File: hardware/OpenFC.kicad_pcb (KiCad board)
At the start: 6 copper layers, 27.6 x 27.6 mm, 135 parts, among them J10 5V, J12 5V, J14 5V, J15 5V, J17 5V, J18 5V, J20 5V, J21 5V, J22 5V, J24 5V, J25 5V, J26 5V, J27 5V, J28 5V, J29 5V, J30 5V, J31 5V, J32 5V, J33 5V, J34 5V, J35 5V, J37 5V, J39 5V, J40 5V, J41 5V, J42 5V, J43 5V, J44 5V, J45 5V, J46 5V, J48 5V, J49 5V, J5 5V, J8 5V, P1 SM08B-SRSS-TB(LF)(SN), Q5 AP1606, Q6 AP1606, U1 COS8051SOT, U10 RP2354A, U11 TS2306A 240GF MSM 9_C2976675, U18 SN74LVC1G3157DTBR, U2 TLV7031DPWR, U3 TI LMR51430YFDDCR, U4 TI LMR51430YFDDCR, U5 TPS2116DRLR, U6 NCV8187AMT180TAG, U7 LP5912-3.3DRVR, U8 SM06B-SRSS-TB(LF)(SN), U9 LSM6DSV16XTR, X1 XTM25012000JT00351001

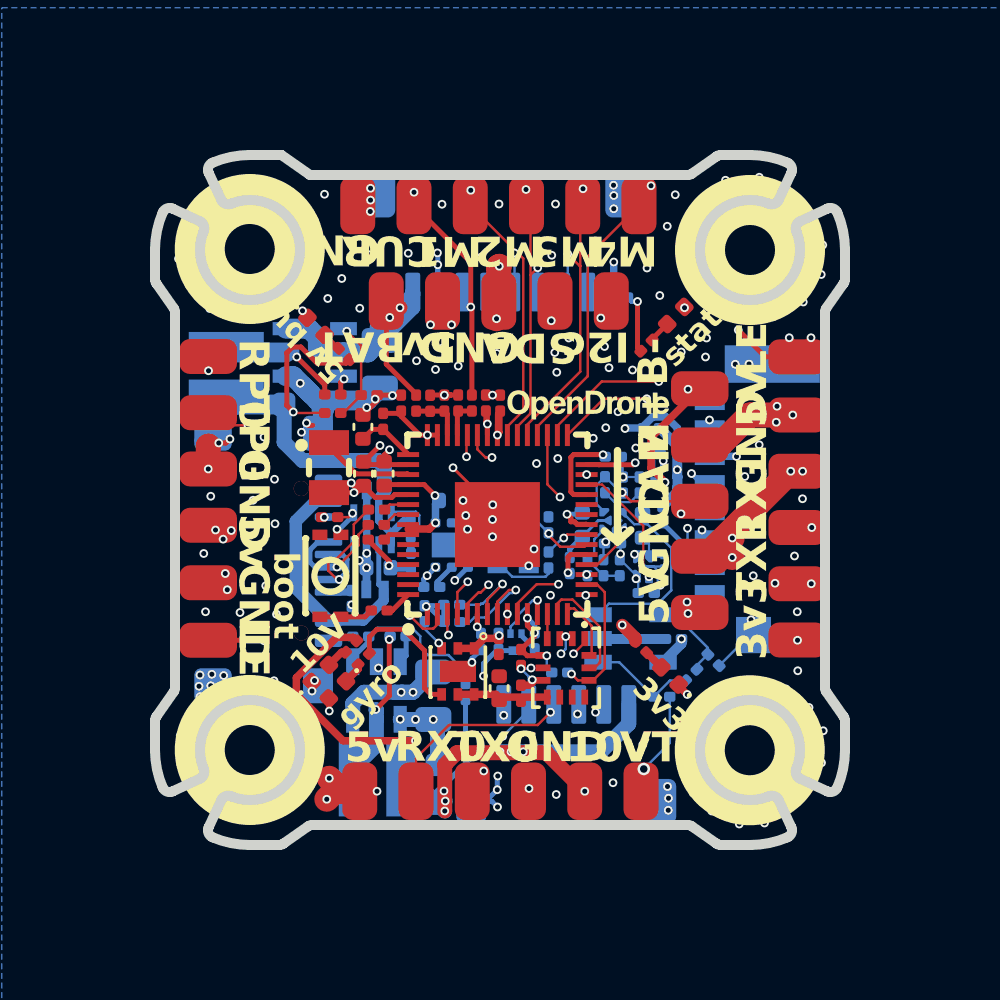
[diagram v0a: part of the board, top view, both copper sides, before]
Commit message: Swap 1.8V LDO and IMU, fix BOM/CPL export hygiene
Part changes, both schematic and PCB:
- U6 NCV8187AMT180TAG (stock 0 at JLC) replaced by U12 LP5912-1.8DRVR
  (C2876234). Same WSON-6 2x2 land pattern as the LP5912-3.3 at U7, so no
  layout change. PG is retained. PSRR at the 1 mA gyro load is ~85 dB to
  1 kHz and ~70 dB at 10 kHz per datasheet Figure 23.
- PG indicator rewired: pull-up from +5V to PG, LED from PG to GND, so the
  LED lights when the rail is good instead of when it has failed.
- U9 LSM6DSV16XTR replaced by BMI270 (C2836813). Bosch Table 22 matches the
  existing LGA-14 symbol pin for pin, so no rewire and no CPL rotation change.
- C33, C34 22uF 0402 moved from C105226 to C415703.

Export fixes:
- U12 carried its part number in a field named "LCSC Part" rather than
  "LCSC", so it exported with no part number and would have been quoted
  unsourced. Renamed.
- The 34 solder pad and testpoint footprints now carry exclude_from_bom
  plus exclude_from_pos_files instead of relying on the dnp flag. They stay
  on the board as copper but no longer need --exclude-dnp at export time.

BOM and CPL now agree at 101 placements with no blank part numbers, exported
without any dnp flag. ERC is unchanged against HEAD (170 vs 171 violations,
all pre-existing).

Co-Authored-By: Claude Fable 5 <noreply@anthropic.com>
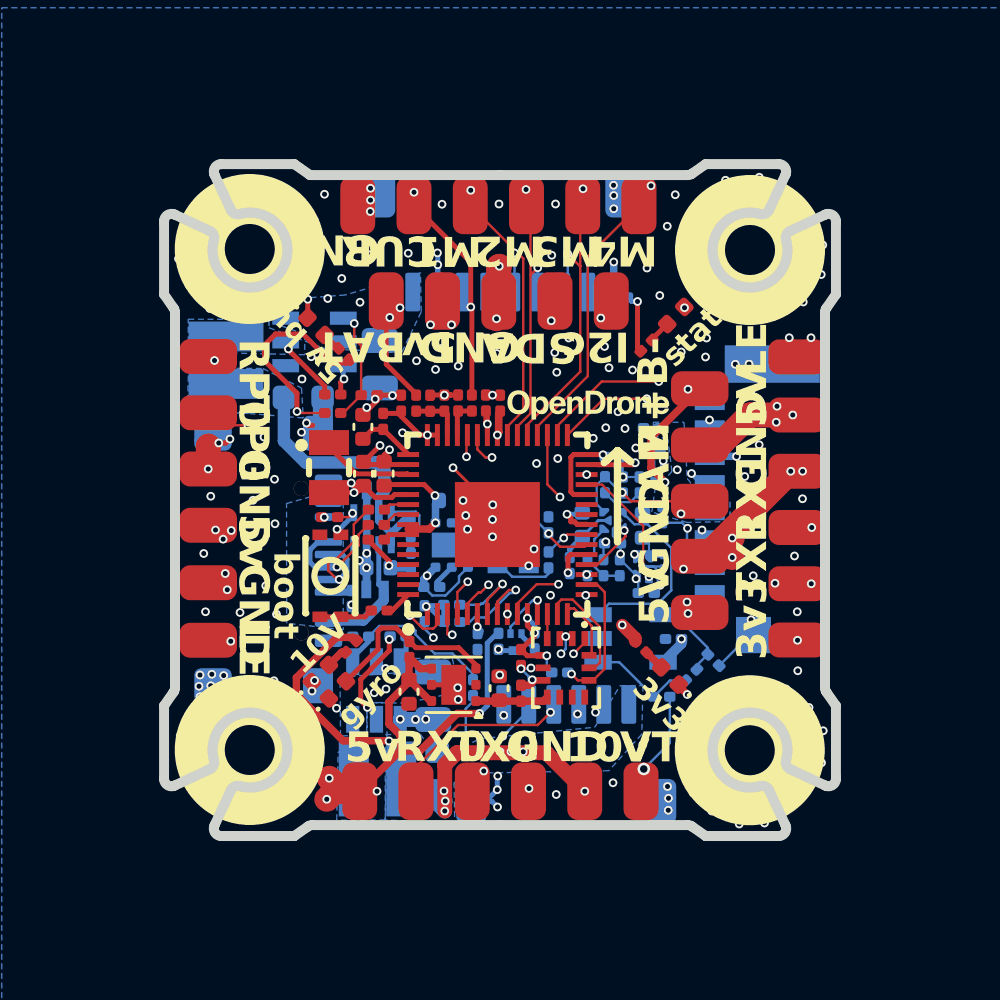
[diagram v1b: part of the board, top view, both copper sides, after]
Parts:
- removed R40: 2.4k, Resistor_SMD:R_0201_0603Metric
- removed U6: NCV8187AMT180TAG, lib:WDFN-6_L2.0-W2.0-P0.65-BL-EP
- added R34: 6.49k, Resistor_SMD:R_0201_0603Metric, F.Cu at (149.0, 92.5)
- added U12: LP5912-1.8DRVR, lib:WSON-6-1EP_2x2mm_P0.65mm_EP1x1.6mm_ThermalVias, F.Cu at (150.8, 93.9)
- C31: value 100n -> 4.7uF; footprint Capacitor_SMD:C_0201_0603Metric -> Capacitor_SMD:C_0402_1005Metric
- U9: value LSM6DSV16XTR -> BMI270
- moved C31 4.02 mm to (149.0, 94.2)
- moved C28 0.53 mm to (150.1, 97.3)
- moved L3 0.42 mm to (141.7, 80.9)
- moved U4 0.42 mm to (145.2, 80.2)
- moved R29 0.34 mm to (151.5, 94.0)
- moved C29 0.28 mm to (144.7, 82.4)
- moved C3 0.14 mm to (151.7, 92.2)
- turned D8 to 45 degrees
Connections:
- D8 pad 1: Net-(D8-K) -> GND
- D8 pad 2: +5V -> /POWER/1.8V_PG
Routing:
- net +BATT: track 39.5 -> 23.9 mm
- net GND: track 94.7 -> 80.3 mm, vias 182 -> 188
- net +10V: track 34.1 -> 19.7 mm
- net +5V: track 38.2 -> 49.5 mm, vias 21 -> 18
- net +5V_USB: track 11.0 -> 4.85 mm
- net +3.3V: track 43.2 -> 37.9 mm
- net /PADS/LED_STRIP: track 57.8 -> 54.0 mm, vias 5 -> 4
- net Net-(U3-SW): track 6.33 -> 3.44 mm
- net Net-(U4-SW): track 4.45 -> 2.42 mm
- net /POWER/1.8V_PG: track 5.64 -> 7.26 mm
- net /BLACKBOX/FLASH_CS: track 13.7 -> 12.2 mm
- net Net-(D8-K): track 0.86 -> 0.00 mm
- net +1.8V_GYRO: track 3.62 -> 2.92 mm
- net Net-(U4-CB): track 0.67 -> 1.22 mm
- net +5V_BUCK: track 19.5 -> 19.0 mm
- added copper zone on B.Cu, net +10V
- added copper zone on B.Cu, net +3.3V
- added copper zone on B.Cu, net +5V_BUCK
- added copper zone on B.Cu, net +5V_USB
- added copper zone on B.Cu, net +BATT
- added copper zone on B.Cu, net Net-(U3-SW)
- added copper zone on B.Cu, net Net-(U4-SW)
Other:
- board size 27.6 x 27.6 mm -> 26.9 x 26.9 mm

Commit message: Rev 3: LP5912 gyro LDO, BMI270
Gyro supply moves to LP5912-1.8DRVR (U12, C2876234); the NCV8187AMT180TAG is
gone from schematic and board. IMU is BMI270 (U9). Bucks stay LMR51430YFDDCR,
which has adequate margin for the 6S ceiling this board shares with the 20x20
ESC.

ERC and DRC reviewed by the maintainer.

Co-Authored-By: Claude Opus 5 (1M context) <noreply@anthropic.com>
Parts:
- U3, U4: value TI LMR51430YFDDCR -> LMR51430YFDDCR
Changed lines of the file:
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@@
 			)
 		)
-		(attr smd exclude_from_pos_files exclude_from_bom)
+		(attr smd exclude_from_bom dnp)
 		(duplicate_pad_numbers_are_jumpers no)
 		(fp_text user "${REFERENCE}"
@@
 			)
 		)
-		(attr smd exclude_from_pos_files exclude_from_bom)
+		(attr smd exclude_from_bom dnp)
 		(duplicate_pad_numbers_are_jumpers no)
 		(fp_text user "${REFERENCE}"
@@
 			)
 		)
-		(attr smd exclude_from_pos_files exclude_from_bom)
+		(attr smd exclude_from_bom dnp)
 		(duplicate_pad_numbers_are_jumpers no)
 		(fp_text user "${REFERENCE}"
@@
 			)
 		)
-		(attr smd exclude_from_pos_files exclude_from_bom)
+		(attr smd exclude_from_bom dnp)
 		(duplicate_pad_numbers_are_jumpers no)
 		(fp_text user "${REFERENCE}"
@@
 			)
 		)
-		(attr smd exclude_from_pos_files exclude_from_bom)
+		(attr smd exclude_from_bom dnp)
 		(duplicate_pad_numbers_are_jumpers no)
 		(fp_text user "${REFERENCE}"
@@
 			)
 		)
-		(attr smd exclude_from_pos_files exclude_from_bom)
+		(attr smd exclude_from_bom dnp)
 		(duplicate_pad_numbers_are_jumpers no)
 		(fp_text user "${REFERENCE}"
@@
 			)
 		)
-		(attr smd exclude_from_pos_files exclude_from_bom)
+		(attr smd exclude_from_bom dnp)
 		(duplicate_pad_numbers_are_jumpers no)
 		(fp_text user "${REFERENCE}"
@@
 			)
 		)
-		(attr smd exclude_from_pos_files exclude_from_bom)
+		(attr smd exclude_from_bom dnp)
 		(duplicate_pad_numbers_are_jumpers no)
 		(fp_text user "${REFERENCE}"
@@
 			)
 		)
-		(attr smd exclude_from_pos_files exclude_from_bom)
+		(attr smd exclude_from_bom dnp)
 		(duplicate_pad_numbers_are_jumpers no)
 		(fp_text user "${REFERENCE}"
@@
 			)
 		)
-		(attr smd exclude_from_pos_files exclude_from_bom)
+		(attr smd exclude_from_bom dnp)
 		(duplicate_pad_numbers_are_jumpers no)
 		(fp_text user "${REFERENCE}"
@@
 			)
 		)
-		(attr smd exclude_from_pos_files exclude_from_bom)
+		(attr smd exclude_from_bom dnp)
 		(duplicate_pad_numbers_are_jumpers no)
 		(fp_text user "${REFERENCE}"
@@
 			)
 		)
-		(attr smd exclude_from_pos_files exclude_from_bom)
+		(attr smd exclude_from_bom dnp)
 		(duplicate_pad_numbers_are_jumpers no)
 		(fp_text user "${REFERENCE}"
@@
 			)
 		)
+		(property "LCSC" "C2876234"
+			(at 0 0 180)
+			(unlocked yes)
+			(layer "F.Fab")
+			(hide yes)
+			(effects
+				(font
+					(size 1 1)
+					(thickness 0.15)
+				)
+			)
+		)
 		(sheetname "/POWER/")
 		(sheetfile "power.kicad_sch")
@@
 			)
 		)
-		(attr smd exclude_from_pos_files exclude_from_bom)
+		(attr smd exclude_from_bom dnp)
 		(duplicate_pad_numbers_are_jumpers no)
 		(fp_text user "${REFERENCE}"
@@
 			)
 		)
-		(attr smd exclude_from_pos_files exclude_from_bom)
+		(attr smd exclude_from_bom dnp)
 		(duplicate_pad_numbers_are_jumpers no)
 		(fp_text user "${REFERENCE}"
@@
 			)
 		)
-		(attr smd exclude_from_pos_files exclude_from_bom)
+		(attr smd exclude_from_bom dnp)
 		(duplicate_pad_numbers_are_jumpers no)
 		(fp_text user "${REFERENCE}"
@@
 			)
 		)
-		(attr smd exclude_from_pos_files exclude_from_bom)
+		(attr smd exclude_from_bom dnp)
 		(duplicate_pad_numbers_are_jumpers no)
 		(fp_text user "${REFERENCE}"
@@
 			)
 		)
-		(attr smd exclude_from_pos_files exclude_from_bom)
+		(attr smd exclude_from_bom dnp)
 		(duplicate_pad_numbers_are_jumpers no)
 		(fp_text user "${REFERENCE}"
@@
 			)
 		)
-		(attr smd exclude_from_pos_files exclude_from_bom)
+		(attr smd exclude_from_bom dnp)
 		(duplicate_pad_numbers_are_jumpers no)
 		(fp_text user "${REFERENCE}"
@@
 			)
 		)
-		(attr smd exclude_from_pos_files exclude_from_bom)
+		(attr smd exclude_from_bom dnp)
 		(duplicate_pad_numbers_are_jumpers no)
 		(fp_text user "${REFERENCE}"
@@
 			)
 		)
-		(attr smd exclude_from_pos_files exclude_from_bom)
+		(attr smd exclude_from_bom dnp)
 		(duplicate_pad_numbers_are_jumpers no)
 		(fp_text user "${REFERENCE}"
@@
 			)
 		)
-		(attr smd exclude_from_pos_files exclude_from_bom)
+		(attr smd exclude_from_bom dnp)
 		(duplicate_pad_numbers_are_jumpers no)
 		(fp_text user "${REFERENCE}"
@@
 			)
 		)
-		(attr smd exclude_from_pos_files exclude_from_bom)
+		(attr smd exclude_from_bom dnp)
 		(duplicate_pad_numbers_are_jumpers no)
 		(fp_text user "${REFERENCE}"
@@
 			)
 		)
-		(attr smd exclude_from_pos_files exclude_from_bom)
+		(attr smd exclude_from_bom dnp)
 		(duplicate_pad_numbers_are_jumpers no)
 		(fp_text user "${REFERENCE}"
@@
 			)
 		)
-		(attr smd exclude_from_pos_files exclude_from_bom)
+		(attr smd exclude_from_bom dnp)
 		(duplicate_pad_numbers_are_jumpers no)
 		(fp_text user "${REFERENCE}"
@@
 			)
 		)
-		(attr smd exclude_from_pos_files exclude_from_bom)
+		(attr smd exclude_from_bom dnp)
 		(duplicate_pad_numbers_are_jumpers no)
 		(fp_text user "${REFERENCE}"
@@
 			)
 		)
-		(attr smd exclude_from_pos_files exclude_from_bom)
+		(attr smd exclude_from_bom dnp)
 		(duplicate_pad_numbers_are_jumpers no)
 		(fp_text user "${REFERENCE}"
@@
 			)
 		)
-		(attr smd exclude_from_pos_files exclude_from_bom)
+		(attr smd exclude_from_bom dnp)
 		(duplicate_pad_numbers_are_jumpers no)
 		(fp_text user "${REFERENCE}"
@@
 			)
 		)
-		(attr smd exclude_from_pos_files exclude_from_bom)
+		(attr smd exclude_from_bom dnp)
 		(duplicate_pad_numbers_are_jumpers no)
 		(fp_text user "${REFERENCE}"
@@
 			)
 		)
-		(attr smd exclude_from_pos_files exclude_from_bom)
+		(attr smd exclude_from_bom dnp)
 		(duplicate_pad_numbers_are_jumpers no)
 		(fp_text user "${REFERENCE}"
@@
 			)
 		)
-		(attr smd exclude_from_pos_files exclude_from_bom)
+		(attr smd exclude_from_bom dnp)
 		(duplicate_pad_numbers_are_jumpers no)
 		(fp_text user "${REFERENCE}"
@@
 			)
 		)
-		(attr smd exclude_from_pos_files exclude_from_bom)
+		(attr smd exclude_from_bom dnp)
 		(duplicate_pad_numbers_are_jumpers no)
 		(fp_text user "${REFERENCE}"
@@
 			)
 		)
-		(attr smd exclude_from_pos_files exclude_from_bom)
+		(attr smd exclude_from_bom dnp)
 		(duplicate_pad_numbers_are_jumpers no)
 		(fp_text user "${REFERENCE}"
@@
 			)
 		)
-		(attr smd exclude_from_pos_files exclude_from_bom)
+		(attr smd exclude_from_bom dnp)
 		(duplicate_pad_numbers_are_jumpers no)
 		(fp_text user "${REFERENCE}"
@@
 			)
 		)
-		(attr smd exclude_from_pos_files exclude_from_bom)
+		(attr smd exclude_from_bom dnp)
 		(duplicate_pad_numbers_are_jumpers no)
 		(fp_text user "${REFERENCE}"
@@
 			)
 		)
-		(property "Value" "TI LMR51430YFDDCR"
+		(property "Value" "LMR51430YFDDCR"
 			(at 0 -5.15 90)
 			(layer "B.Fab")
@@
 			)
 		)
-		(property "LCSC" "C5219261"
+		(property "LCSC" "C45262770"
 			(at 0 0 270)
 			(unlocked yes)
@@
 			)
 		)
-		(property "MPN" "TI LMR51430YFDDCR"
+		(property "MPN" "LMR51430YFDDCR"
 			(at 0 0 270)
 			(unlocked yes)
@@
 		(model "${KIPRJMOD}/lib.3dshapes/DFN-3L_L1.0-W0.6-H0.5-P0.65-BR.wrl"
 			(offset
-				(xyz 0.01 -0 0.5)
+				(xyz 0.01 0 0)
 			)
 			(scale
@@
 			)
 		)
-		(property "Value" "TI LMR51430YFDDCR"
+		(property "Value" "LMR51430YFDDCR"
 			(at 0 -5.15 0)
 			(layer "B.Fab")
@@
 			)
 		)
-		(property "LCSC" "C5219261"
+		(property "LCSC" "C45262770"
 			(at 0 0 0)
 			(unlocked yes)
@@
 			)
 		)
-		(property "MPN" "TI LMR51430YFDDCR"
+		(property "MPN" "LMR51430YFDDCR"
 			(at 0 0 0)
 			(unlocked yes)
@@
 		(model "${KIPRJMOD}/lib.3dshapes/SOD-882_L1.0-W0.6-H0.5-LS0.65.wrl"
 			(offset
-				(xyz -911.61 887.73 0)
+				(xyz 0 0 0)
 			)
 			(scale
@@
 		(model "${KIPRJMOD}/lib.3dshapes/SOD-882_L1.0-W0.6-H0.5-LS0.65.wrl"
 			(offset
-				(xyz -911.61 887.73 0)
+				(xyz 0 0 0)
 			)
 			(scale

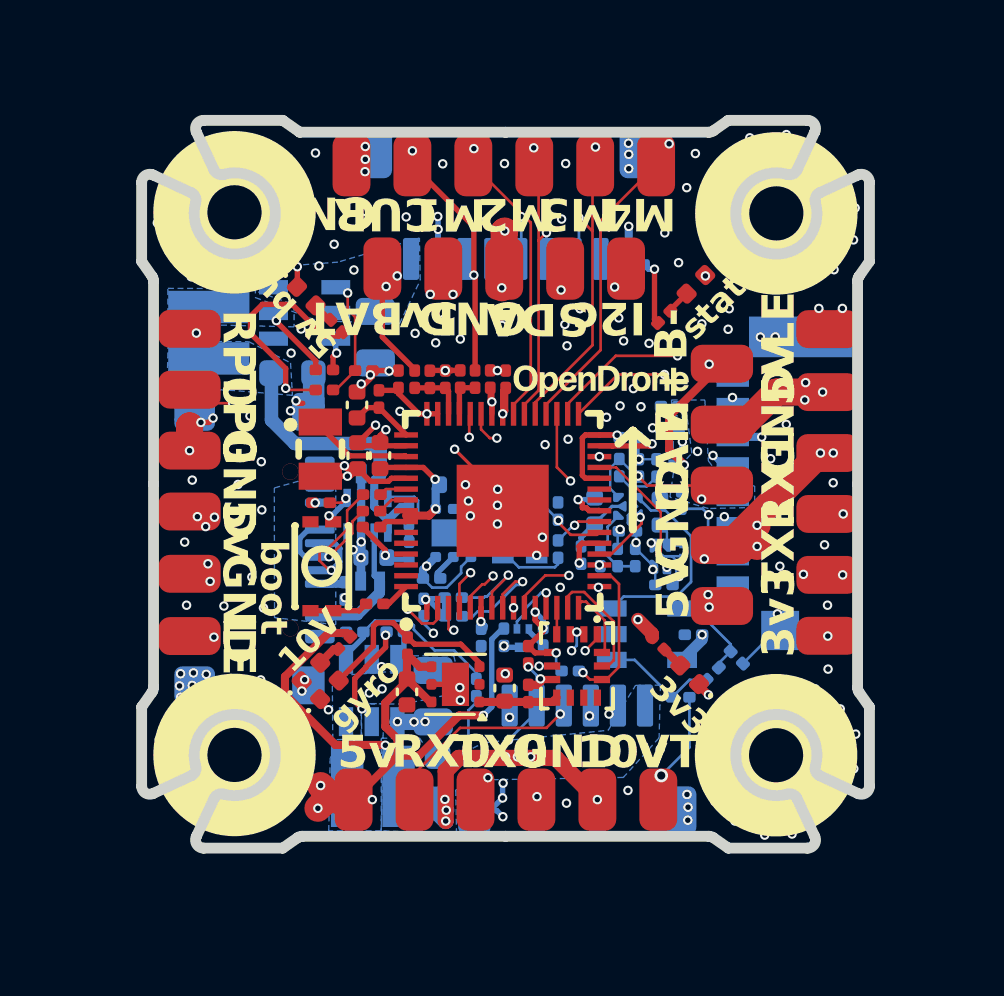
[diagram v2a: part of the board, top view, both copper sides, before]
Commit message: 4V5 rework: TPS2116 mux replaced by DSK24 diode-OR
U5, its diodes, R27/R28 and C30 removed. D6 from the buck output and
D10 from +5V_USB feed the new +4v5 net for the LDOs, JST and pads; the
buck output is plain +5V to the external pads. DSK24 footprint and 3D
model committed with the change. Shop badge gold.

Co-Authored-By: Claude Opus 5 (1M context) <noreply@anthropic.com>
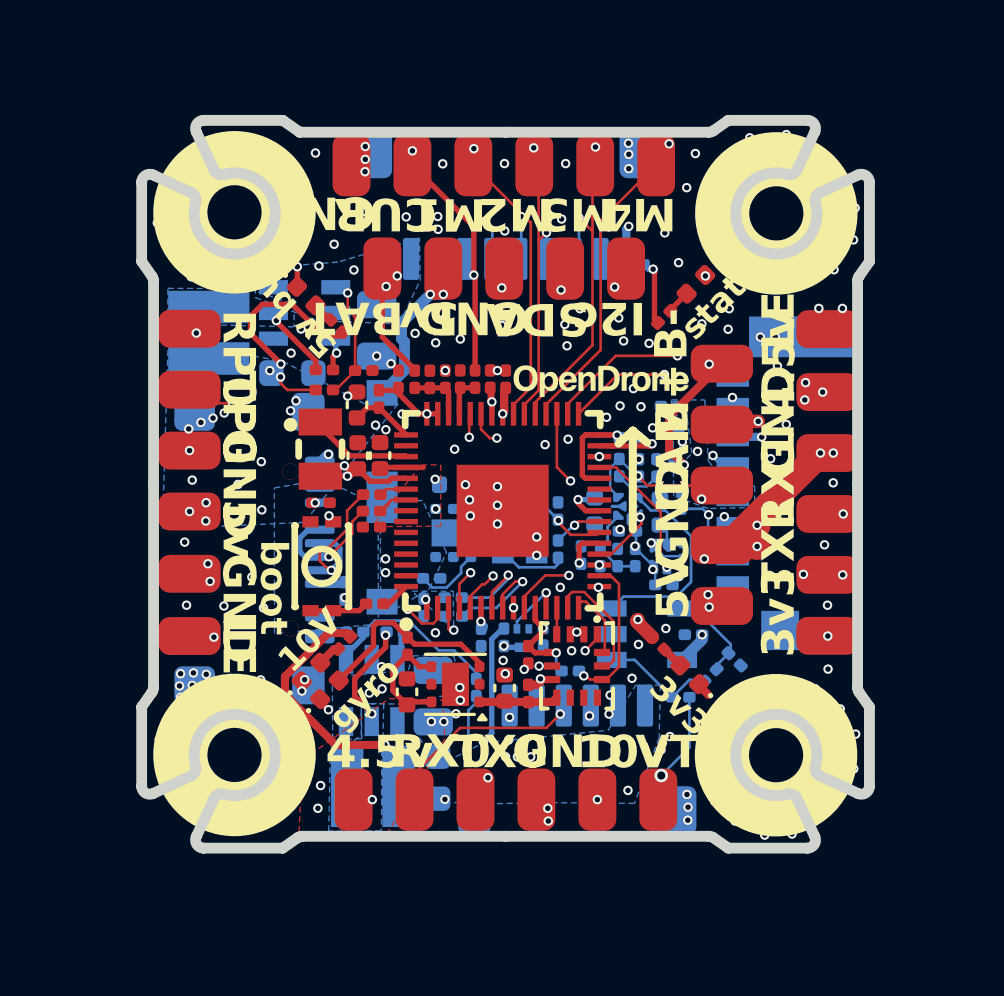
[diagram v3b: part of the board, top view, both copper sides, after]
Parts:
- removed C30: 4.7uF, Capacitor_SMD:C_0402_1005Metric
- removed D3: RB161QS-40_C28646385, lib:SOD-882_L1.0-W0.6-RD
- removed R27: 100k, Resistor_SMD:R_0201_0603Metric
- removed R28: 39k, Resistor_SMD:R_0201_0603Metric
- removed U5: TPS2116DRLR, lib:SOT-583-8_L2.1-W1.6-P0.50-LS1.6-BL
- added D6: DSK24, lib:SOD-123_L2.8-W1.8-LS3.7-RD, B.Cu at (148.1, 84.8)
- D10: value RB161QS-40_C28646385 -> DSK24; footprint lib:SOD-882_L1.0-W0.6-RD -> lib:SOD-123_L2.8-W1.8-LS3.7-RD
- moved D10 1.03 mm to (148.1, 89.2), turned to -90 degrees
- moved C25 0.25 mm to (147.8, 80.8)
- moved R46 0.11 mm to (161.1, 93.0)
- moved R47 0.10 mm to (160.2, 93.6)
- turned C31 to 90 degrees
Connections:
- C29 pad 1: +5V_BUCK -> +5V
- C31 pad 1: +5V -> +4v5
- C32 pad 1: +5V -> +4v5
- D10 pad 1: +5V -> +4v5
- J40 pad 1: +5V -> +4v5
- J5 pad 1: +5V -> +4v5
- L3 pad 2: +5V_BUCK -> +5V
- R31 pad 2: +5V_BUCK -> +5V
- R34 pad 1: +5V -> +4v5
- R50 pad 1: +5V_BUCK -> +5V
- U12 pad 4: +5V -> +4v5
- U12 pad 6: +5V -> +4v5
- U7 pad 4: +5V -> +4v5
- U7 pad 6: +5V -> +4v5
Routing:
- net +4v5: track 0.00 -> 51.4 mm, vias 0 -> 8
- net GND: track 80.3 -> 31.3 mm, vias 188 -> 187
- net +5V: track 49.5 -> 22.1 mm, vias 18 -> 12
- net +5V_BUCK: track 19.0 -> 0.00 mm, vias 1 -> 0
- net +10V: track 19.7 -> 10.7 mm, vias 8 -> 6
- net +3.3V: track 37.9 -> 29.8 mm, vias 16 -> 15
- net +5V_USB: track 4.85 -> 0.00 mm
- net Net-(U5-PR1): track 2.86 -> 0.00 mm
- added copper zone on F.Cu, net +3.3V
- added copper zone on B.Cu, net +4v5
- added copper zone on F.Cu, net +4v5
- added copper zone on B.Cu, net +5V
- removed copper zone on B.Cu, net +5V_BUCK
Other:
- board text added: "4.5v"

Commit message: Rebuild E6 substitute STEP models from the trusted wrl geometry
The .step files beside these .wrl models were different parts (USB-C
3.5x oversized, etc), and the upstream LCSC .step is the same wrong
file, so kicad-cli --subst-models shipped wrong geometry in every STEP
export while the 3D viewer looked perfect. Rebuilt as tessellated STEP
solids from the .wrl the viewer renders, via
OpenDrone-Scripts/kicad/wrl_to_step.py: bbox and origin now match to
0.000 mm. check_models reports zero E6, export unblocked.

Co-Authored-By: Claude Opus 5 (1M context) <noreply@anthropic.com>
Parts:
- moved C28 0.14 mm to (150.1, 97.2)
- moved R31 0.09 mm to (145.9, 82.9)
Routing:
- net GND: track 31.3 -> 20.9 mm, vias 187 -> 196
- net +5V: track 22.1 -> 14.9 mm
- net +1.1V: track 29.6 -> 27.1 mm
- net +3.3V: track 29.8 -> 31.5 mm
- net +BATT: track 23.9 -> 23.2 mm
- added copper zone on F.Cu, net +1.1V
- added copper zone on F.Cu, net Net-(U10-VREG_LX)
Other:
- board text added: "REV3.1"
